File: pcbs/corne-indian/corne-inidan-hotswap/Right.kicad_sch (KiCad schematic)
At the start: 51 parts, among them SW1 SW_Push, SW10 SW_Push, SW11 SW_Push, SW12 SW_Push, SW13 SW_Push, SW14 SW_Push, SW15 SW_Push, SW16 SW_Push, SW17 SW_Push, SW18 SW_Push, SW19 SW_Push, SW2 SW_Push, SW20 SW_Push, SW21 SW_Push, SW3 SW_Push, SW4 SW_Push, SW5 SW_Push, SW6 SW_Push, SW7 SW_Push, SW8 SW_Push, SW9 SW_Push

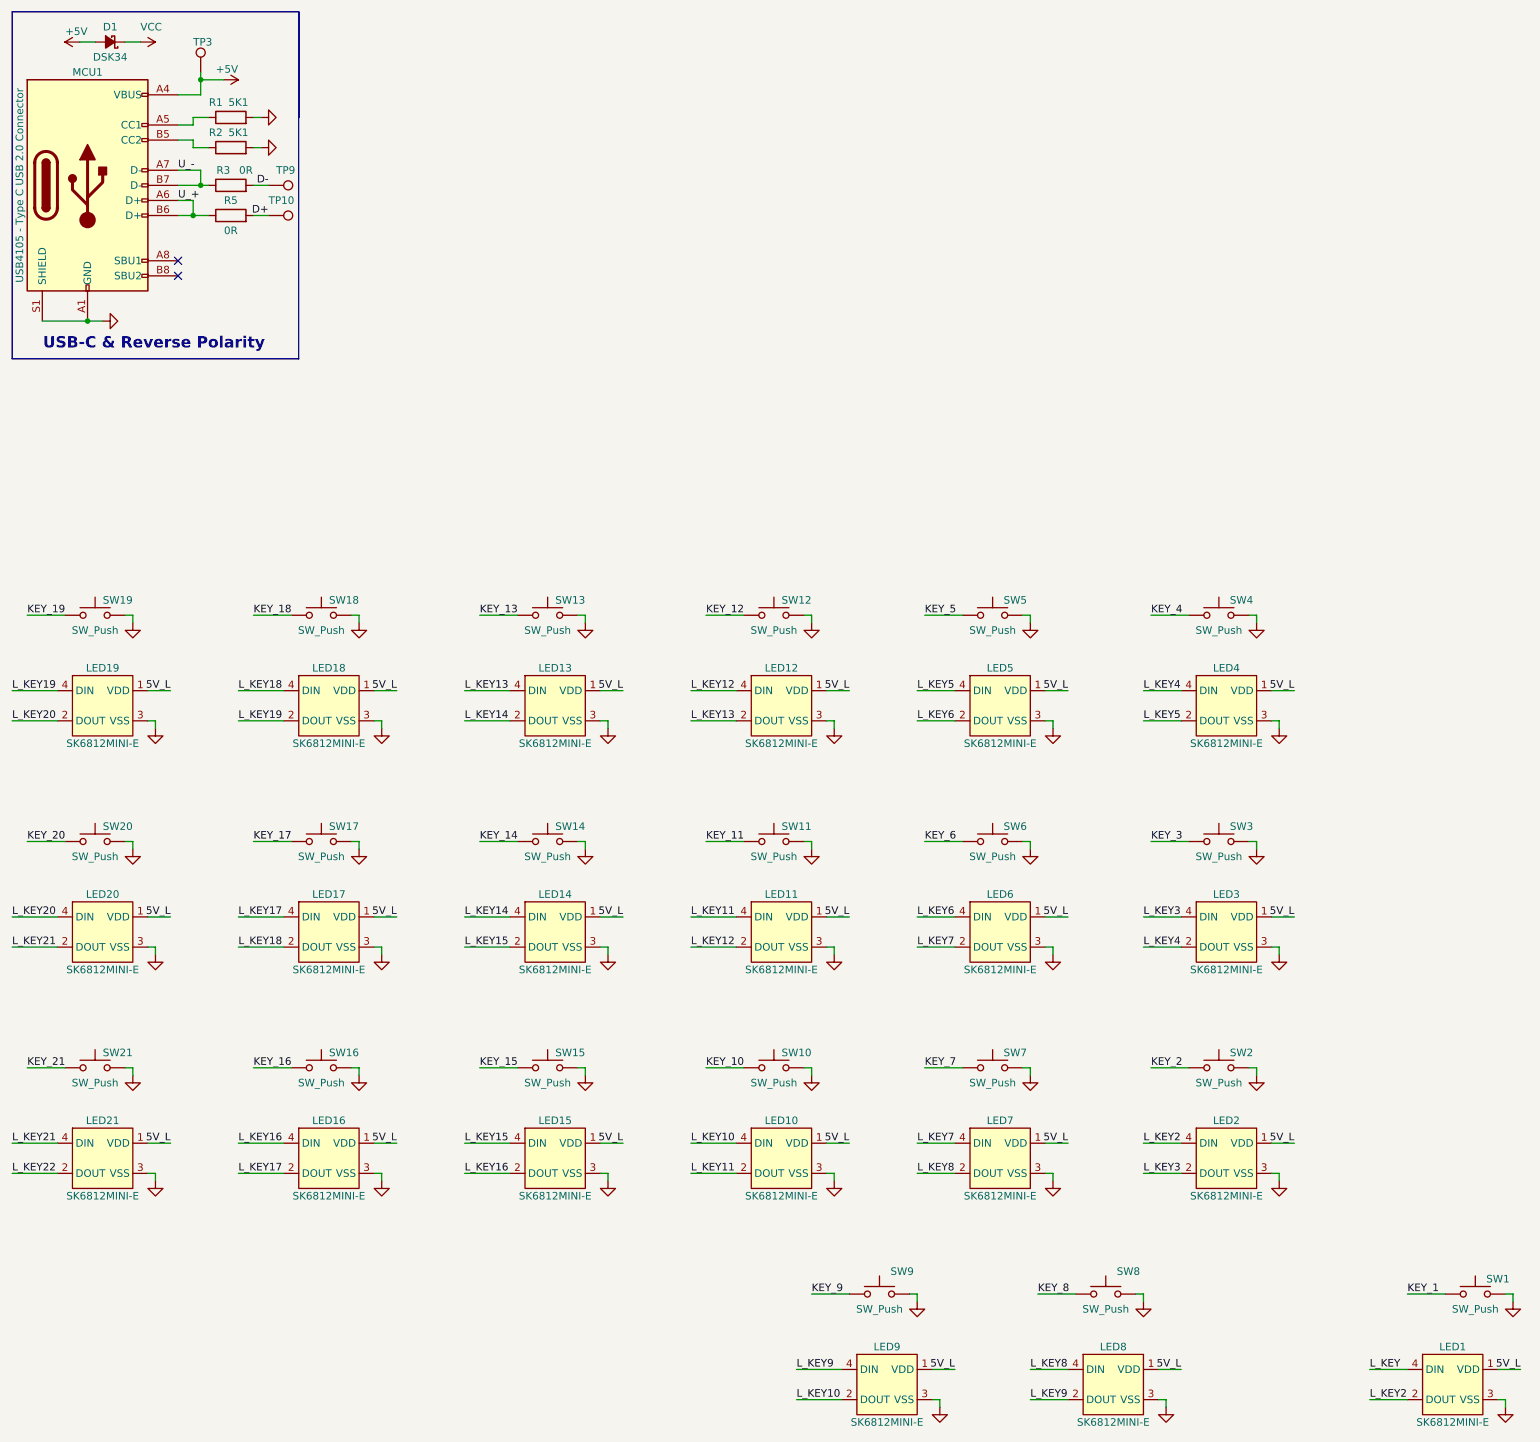
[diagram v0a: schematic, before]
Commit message: Schematic is Done for Right side But Only switch & LED & placement
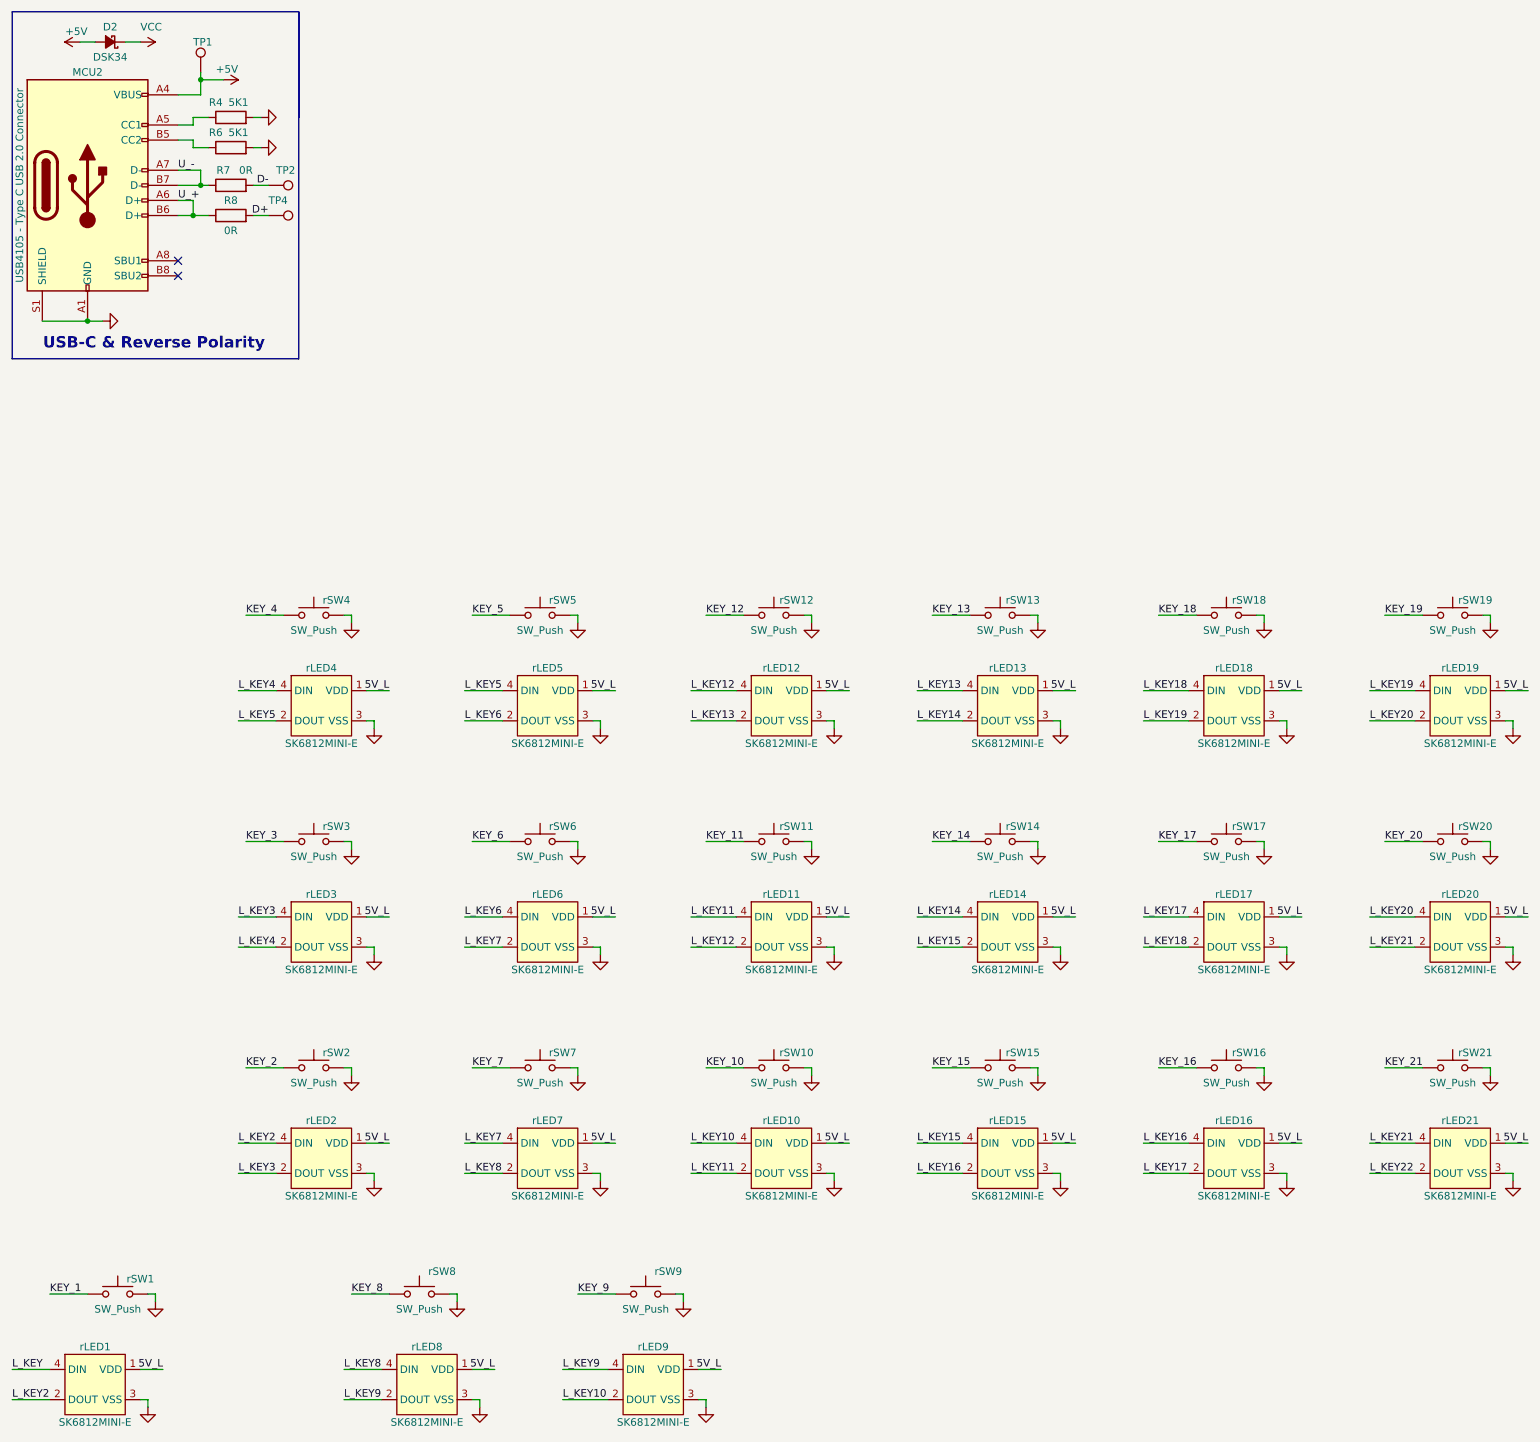
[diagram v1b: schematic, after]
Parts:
- removed D1: DSK34, Diode_SMD:D_SOD-123F, symbol Device:D_Schottky_Small_Filled
- removed LED10, LED11, LED12, LED13, LED14, LED15, LED16, LED17, LED18, LED19, LED2, LED20, LED21, LED3, LED4, LED5, LED6, LED7, LED8, LED9: SK6812MINI-E, User_Button_Switch_Keyboard:YS-SK6812MINI-E, symbol LED_RGB:LED_SK6812MINI-E
- removed MCU1: USB4105 - Type C USB 2.0 Connector, Connector_USB:USB_C_Receptacle_GCT_USB4105-xx-A_16P_TopMnt_Horizontal, symbol Connector:USB_C_Receptacle_USB2.0_16P
- removed R1, R2: 5K1, Resistor_SMD:R_0603_1608Metric, symbol Device:R
- removed R3, R5: 0R, Resistor_SMD:R_0603_1608Metric, symbol Device:R
- removed SW1: SW_Push, User_Button_Switch_Keyboard:SW_Cherry_MX_1.50u_Hotswap, symbol Switch:SW_Push
- removed SW10, SW11, SW12, SW13, SW14, SW15, SW16, SW17, SW18, SW19, SW2, SW20, SW21, SW3, SW4, SW5, SW6, SW7, SW8, SW9: SW_Push, User_Button_Switch_Keyboard:SW_Cherry_MX_1.00u_Hotswap, symbol Switch:SW_Push
- removed TP10, TP3, TP9: TestPoint, TestPoint:TestPoint_Pad_D1.0mm, symbol Connector:TestPoint
- added D2: DSK34, Diode_SMD:D_SOD-123F, symbol Device:D_Schottky_Small_Filled
- added MCU2: USB4105 - Type C USB 2.0 Connector, Connector_USB:USB_C_Receptacle_GCT_USB4105-xx-A_16P_TopMnt_Horizontal, symbol Connector:USB_C_Receptacle_USB2.0_16P
- added R4, R6: 5K1, Resistor_SMD:R_0603_1608Metric, symbol Device:R
- added R7, R8: 0R, Resistor_SMD:R_0603_1608Metric, symbol Device:R
- added TP1, TP2, TP4: TestPoint, TestPoint:TestPoint_Pad_D1.0mm, symbol Connector:TestPoint
- added rLED10, rLED11, rLED12, rLED13, rLED14, rLED15, rLED16, rLED17, rLED18, rLED19, rLED2, rLED20, rLED21, rLED3, rLED4, rLED5, rLED6, rLED7, rLED8, rLED9: SK6812MINI-E, User_Button_Switch_Keyboard:YS-SK6812MINI-E, symbol LED_RGB:LED_SK6812MINI-E
- added rSW1: SW_Push, User_Button_Switch_Keyboard:SW_Cherry_MX_1.50u_Hotswap, symbol Switch:SW_Push
- added rSW10, rSW11, rSW12, rSW13, rSW14, rSW15, rSW16, rSW17, rSW18, rSW19, rSW2, rSW20, rSW21, rSW3, rSW4, rSW5, rSW6, rSW7, rSW8, rSW9: SW_Push, User_Button_Switch_Keyboard:SW_Cherry_MX_1.00u_Hotswap, symbol Switch:SW_Push
- renumbered LED1 to rLED1
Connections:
- net +5V: now also D2.2 (A), MCU2.A4 (VBUS), MCU2.A9 (VBUS), MCU2.B4 (VBUS), MCU2.B9 (VBUS), TP1.1
- net 5V_L: now also rLED10.1 (VDD), rLED11.1 (VDD), rLED12.1 (VDD), rLED13.1 (VDD), rLED14.1 (VDD), rLED15.1 (VDD), rLED16.1 (VDD), rLED17.1 (VDD), rLED18.1 (VDD), rLED19.1 (VDD), rLED2.1 (VDD), rLED20.1 (VDD), rLED21.1 (VDD), rLED3.1 (VDD), rLED4.1 (VDD), rLED5.1 (VDD), rLED6.1 (VDD), rLED7.1 (VDD), rLED8.1 (VDD), rLED9.1 (VDD)
- net D+: now also R8.2, TP4.1
- net D-: now also R7.2, TP2.1
- net GND: now also MCU2.A1 (GND), MCU2.A12 (GND), MCU2.B1 (GND), MCU2.B12 (GND), MCU2.S1 (SHIELD), R4.2, R6.2, rLED10.3 (VSS), rLED11.3 (VSS), rLED12.3 (VSS), rLED13.3 (VSS), rLED14.3 (VSS), rLED15.3 (VSS), rLED16.3 (VSS), rLED17.3 (VSS), rLED18.3 (VSS), rLED19.3 (VSS), rLED2.3 (VSS), rLED20.3 (VSS), rLED21.3 (VSS), rLED3.3 (VSS), rLED4.3 (VSS), rLED5.3 (VSS), rLED6.3 (VSS), rLED7.3 (VSS), rLED8.3 (VSS), rLED9.3 (VSS), rSW1.2, rSW10.2, rSW11.2, rSW12.2, rSW13.2, rSW14.2, rSW15.2, rSW16.2, rSW17.2, rSW18.2, rSW19.2, rSW2.2, rSW20.2, rSW21.2, rSW3.2, rSW4.2, rSW5.2, rSW6.2, rSW7.2, rSW8.2, rSW9.2
- net KEY_1: now also rSW1.1
- net KEY_10: now also rSW10.1
- net KEY_11: now also rSW11.1
- net KEY_12: now also rSW12.1
- net KEY_13: now also rSW13.1
- net KEY_14: now also rSW14.1
- net KEY_15: now also rSW15.1
- net KEY_16: now also rSW16.1
- net KEY_17: now also rSW17.1
- net KEY_18: now also rSW18.1
- net KEY_19: now also rSW19.1
- net KEY_2: now also rSW2.1
- net KEY_20: now also rSW20.1
- net KEY_21: now also rSW21.1
- net KEY_3: now also rSW3.1
- net KEY_4: now also rSW4.1
- net KEY_5: now also rSW5.1
- net KEY_6: now also rSW6.1
- net KEY_7: now also rSW7.1
- net KEY_8: now also rSW8.1
- net KEY_9: now also rSW9.1
- net L_KEY10: now also rLED10.4 (DIN), rLED9.2 (DOUT)
- net L_KEY11: now also rLED10.2 (DOUT), rLED11.4 (DIN)
- net L_KEY12: now also rLED11.2 (DOUT), rLED12.4 (DIN)
- net L_KEY13: now also rLED12.2 (DOUT), rLED13.4 (DIN)
- net L_KEY14: now also rLED13.2 (DOUT), rLED14.4 (DIN)
- net L_KEY15: now also rLED14.2 (DOUT), rLED15.4 (DIN)
- net L_KEY16: now also rLED15.2 (DOUT), rLED16.4 (DIN)
- net L_KEY17: now also rLED16.2 (DOUT), rLED17.4 (DIN)
- net L_KEY18: now also rLED17.2 (DOUT), rLED18.4 (DIN)
- net L_KEY19: now also rLED18.2 (DOUT), rLED19.4 (DIN)
- net L_KEY2: now also rLED2.4 (DIN)
- net L_KEY20: now also rLED19.2 (DOUT), rLED20.4 (DIN)
- net L_KEY21: now also rLED20.2 (DOUT), rLED21.4 (DIN)
- net L_KEY22: now also rLED21.2 (DOUT)
- net L_KEY3: now also rLED2.2 (DOUT), rLED3.4 (DIN)
- net L_KEY4: now also rLED3.2 (DOUT), rLED4.4 (DIN)
- net L_KEY5: now also rLED4.2 (DOUT), rLED5.4 (DIN)
- net L_KEY6: now also rLED5.2 (DOUT), rLED6.4 (DIN)
- net L_KEY7: now also rLED6.2 (DOUT), rLED7.4 (DIN)
- net L_KEY8: now also rLED7.2 (DOUT), rLED8.4 (DIN)
- net L_KEY9: now also rLED8.2 (DOUT), rLED9.4 (DIN)
- net U_+: now also MCU2.A6 (D+), MCU2.B6 (D+), R8.1
- net U_-: now also MCU2.A7 (D-), MCU2.B7 (D-), R7.1
- net VCC: now also D2.1 (K)
- new net: MCU2.A5 (CC1), R4.1
- new net: MCU2.B5 (CC2), R6.1
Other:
- moved on the sheet: rLED1

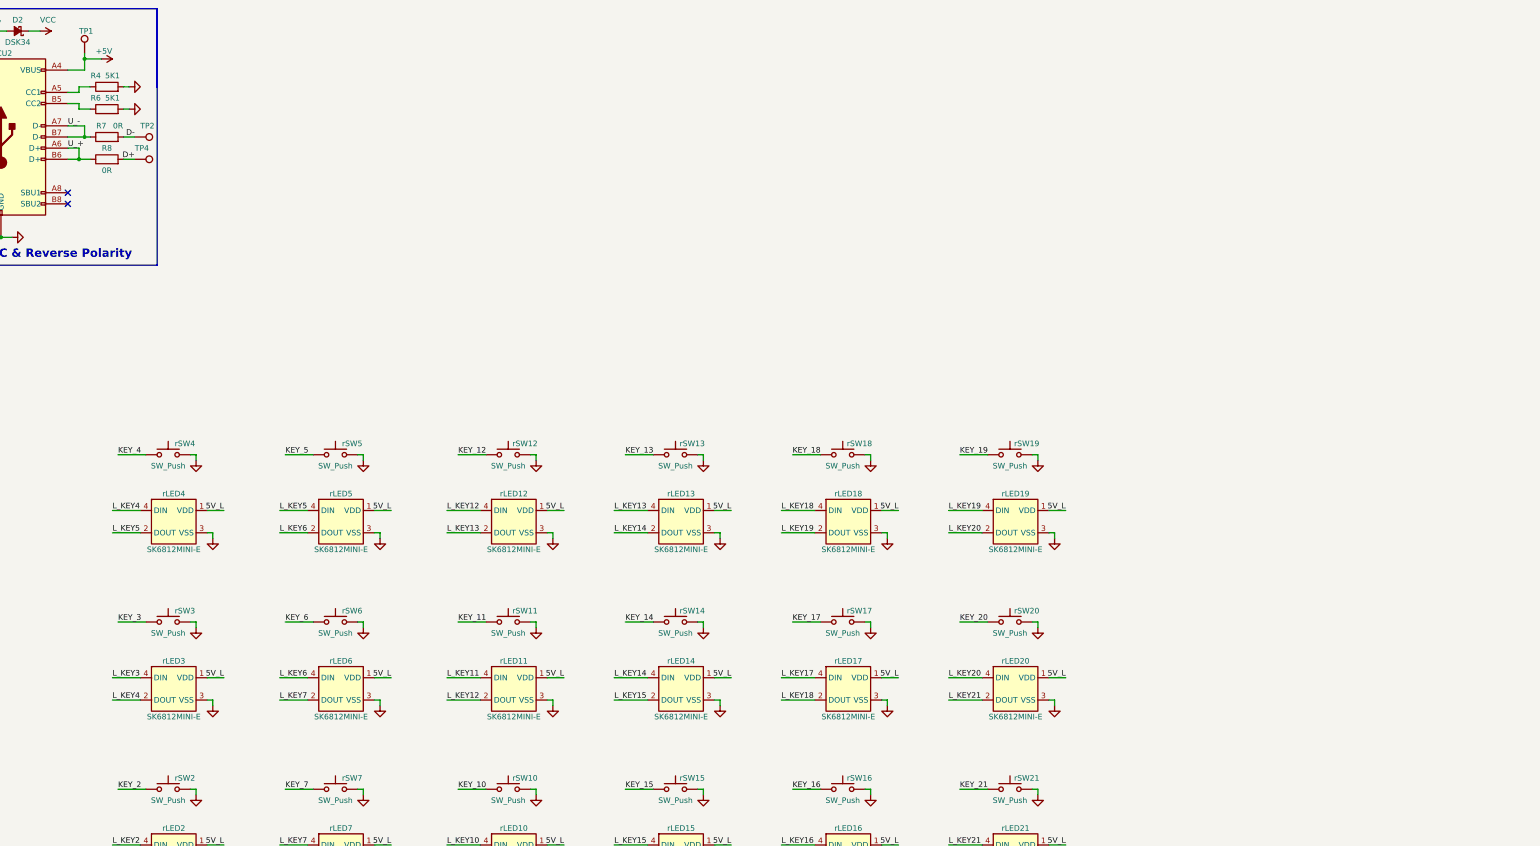
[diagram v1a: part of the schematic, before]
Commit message: Rp2040 added to the shematic need to map to all Key Switch pins
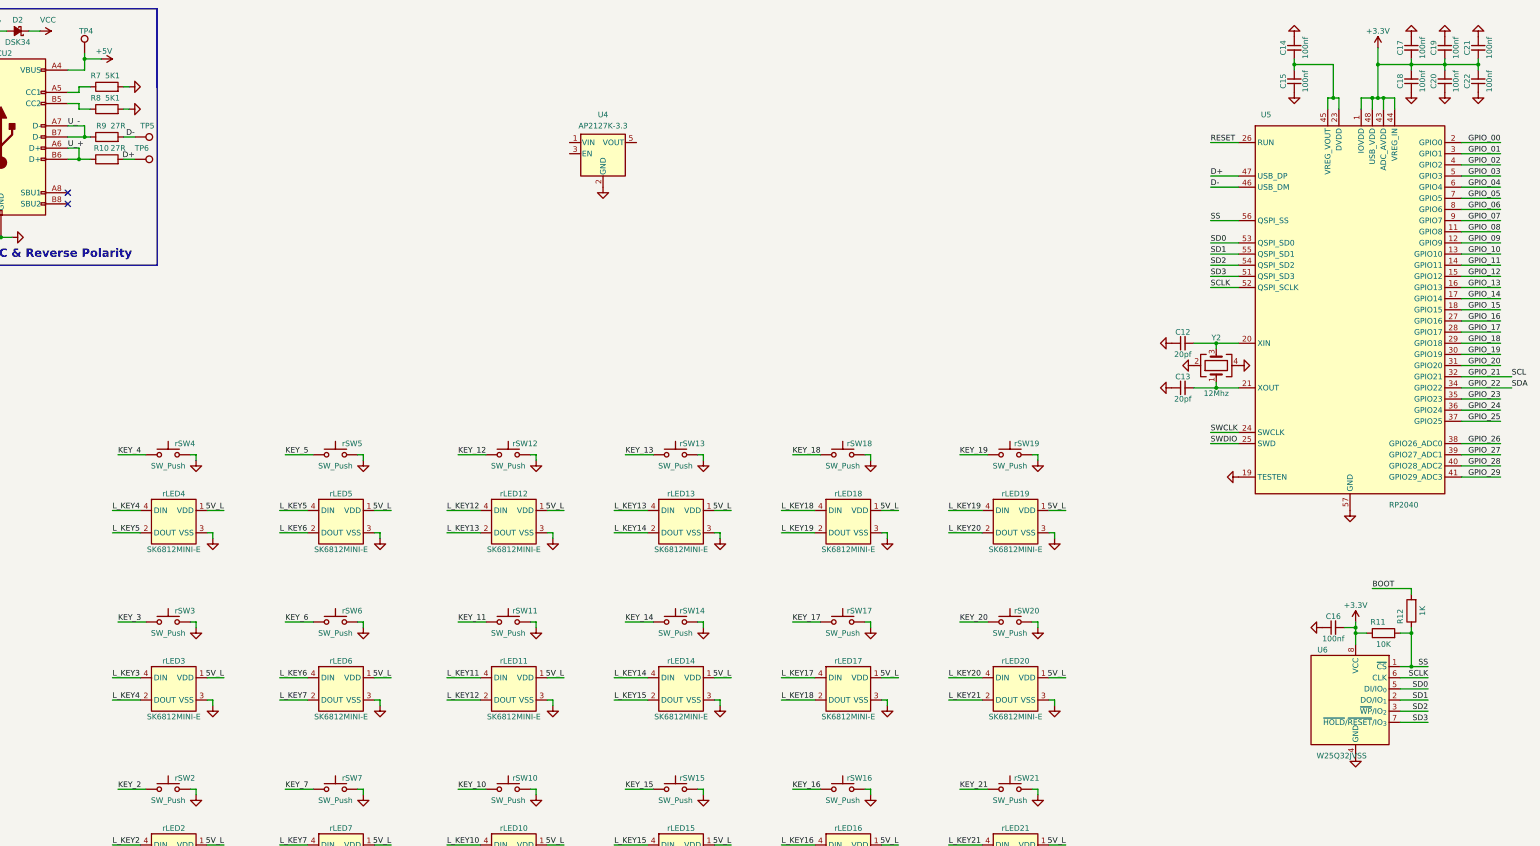
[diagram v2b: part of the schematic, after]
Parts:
- removed R7, R8: 0R, Resistor_SMD:R_0603_1608Metric, symbol Device:R
- added C12, C13: 20pf, Capacitor_SMD:C_0603_1608Metric, symbol Device:C_Small
- added C14, C15, C16, C17, C18, C19, C20, C21, C22: 100nf, Capacitor_SMD:C_0603_1608Metric, symbol Device:C_Small
- added R10, R9: 27R, Resistor_SMD:R_0603_1608Metric, symbol Device:R
- added R11: 10K, Resistor_SMD:R_0603_1608Metric, symbol Device:R
- added R12: 1K, Resistor_SMD:R_0603_1608Metric, symbol Device:R
- added U4: AP2127K-3.3, Package_TO_SOT_SMD:SOT-23-5, symbol Regulator_Linear:AP2127K-3.3
- added U5: RP2040, Package_DFN_QFN:QFN-56-1EP_7x7mm_P0.4mm_EP3.2x3.2mm, symbol MCU_RaspberryPi:RP2040
- added U6: W25Q32JVSS, Package_SO:SOIC-8_5.3x5.3mm_P1.27mm, symbol Memory_Flash:W25Q32JVSS
- added Y2: 12Mhz, Crystal:Crystal_SMD_Abracon_ABM8AIG-4Pin_3.2x2.5mm, symbol Device:Crystal_GND24
- renumbered R4 to R7, R6 to R8, TP1 to TP4, TP2 to TP5, TP4 to TP6
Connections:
- net D+: now also R10.2, U5.47 (USB_DP)
- net D-: now also R9.2, U5.46 (USB_DM)
- net GND: now also C12.1, C13.1, C14.1, C15.1, C16.1, C17.1, C18.1, C19.1, C20.1, C21.1, C22.1, U4.2 (GND), U5.19 (TESTEN), U5.57 (GND), U6.4 (GND), Y2.2, Y2.4
- net U_+: now also R10.1
- net U_-: now also R9.1
- new net: C13.2, U5.21 (XOUT), Y2.1
- new net: C12.2, U5.20 (XIN), Y2.3
- new net: C14.2, C15.2, U5.23 (DVDD), U5.45 (VREG_VOUT), U5.50 (DVDD)
- new net +3.3V: C16.2, C17.2, C18.2, C19.2, C20.2, C21.2, C22.2, R11.1, U5.1 (IOVDD), U5.10 (IOVDD), U5.22 (IOVDD), U5.33 (IOVDD), U5.42 (IOVDD), U5.43 (ADC_AVDD), U5.44 (VREG_IN), U5.48 (USB_VDD), U5.49 (IOVDD), U6.8 (VCC)
- new net BOOT: R12.2
- new net GPIO_00: U5.2 (GPIO0)
- new net GPIO_01: U5.3 (GPIO1)
- new net GPIO_02: U5.4 (GPIO2)
- new net GPIO_03: U5.5 (GPIO3)
- new net GPIO_04: U5.6 (GPIO4)
- new net GPIO_05: U5.7 (GPIO5)
- new net GPIO_06: U5.8 (GPIO6)
- new net GPIO_07: U5.9 (GPIO7)
- new net GPIO_08: U5.11 (GPIO8)
- new net GPIO_09: U5.12 (GPIO9)
- new net GPIO_10: U5.13 (GPIO10)
- new net GPIO_11: U5.14 (GPIO11)
- new net GPIO_12: U5.15 (GPIO12)
- new net GPIO_13: U5.16 (GPIO13)
- new net GPIO_14: U5.17 (GPIO14)
- new net GPIO_15: U5.18 (GPIO15)
- new net GPIO_16: U5.27 (GPIO16)
- new net GPIO_17: U5.28 (GPIO17)
- new net GPIO_18: U5.29 (GPIO18)
- new net GPIO_19: U5.30 (GPIO19)
- new net GPIO_20: U5.31 (GPIO20)
- new net GPIO_21: U5.32 (GPIO21)
- new net GPIO_22: U5.34 (GPIO22)
- new net GPIO_23: U5.35 (GPIO23)
- new net GPIO_24: U5.36 (GPIO24)
- new net GPIO_25: U5.37 (GPIO25)
- new net GPIO_26: U5.38 (GPIO26_ADC0)
- new net GPIO_27: U5.39 (GPIO27_ADC1)
- new net GPIO_28: U5.40 (GPIO28_ADC2)
- new net GPIO_29: U5.41 (GPIO29_ADC3)
- new net RESET: U5.26 (RUN)
- new net SCLK: U5.52 (QSPI_SCLK), U6.6 (CLK)
- new net SD0: U5.53 (QSPI_SD0), U6.5 (DI/IO_{0})
- new net SD1: U5.55 (QSPI_SD1), U6.2 (DO/IO_{1})
- new net SD2: U5.54 (QSPI_SD2), U6.3 (~{WP}/IO_{2})
- new net SD3: U5.51 (QSPI_SD3), U6.7 (~{HOLD}/~{RESET}/IO_{3})
- new net SS: R11.2, R12.1, U5.56 (QSPI_SS), U6.1 (~{CS})
- new net SWCLK: U5.24 (SWCLK)
- new net SWDIO: U5.25 (SWD)
